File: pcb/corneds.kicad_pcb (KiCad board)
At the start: 2 copper layers, 320 x 105.6 mm, 124 parts, among them J3 AudioJack4, J4 AudioJack4, SW1 SW_Push, SW10 SW_Push, SW11 SW_Push, SW12 SW_Push, SW13 SW_Push, SW14 SW_Push, SW15 SW_Push, SW16 SW_Push, SW17 SW_Push, SW18 SW_Push, SW19 SW_Push, SW2 SW_Push, SW20 SW_Push, SW21 SW_Push, SW22 SW_Push, SW23 SW_Push, SW24 SW_Push, SW25 SW_Push, SW26 SW_Push, SW27 SW_Push, SW28 SW_Push, SW29 SW_Push, SW3 SW_Push, SW30 SW_Push, SW31 SW_Push, SW32 SW_Push, SW33 SW_Push, SW34 SW_Push, SW35 SW_Push, SW36 SW_Push, SW37 SW_Push, SW38 SW_Push, SW39 SW_Push, SW4 SW_Push, SW40 SW_Push, SW41 SW_Push, SW42 SW_Push, SW5 SW_Push, SW6 SW_Push, SW7 SW_Push, SW8 SW_Push, SW9 SW_Push, U1 Pico, U2 Pico, U3 SWD_Connector_3pin, U4 SWD_Connector_3pin, U5 Debug_UART_l, U6 Debug_UART_r

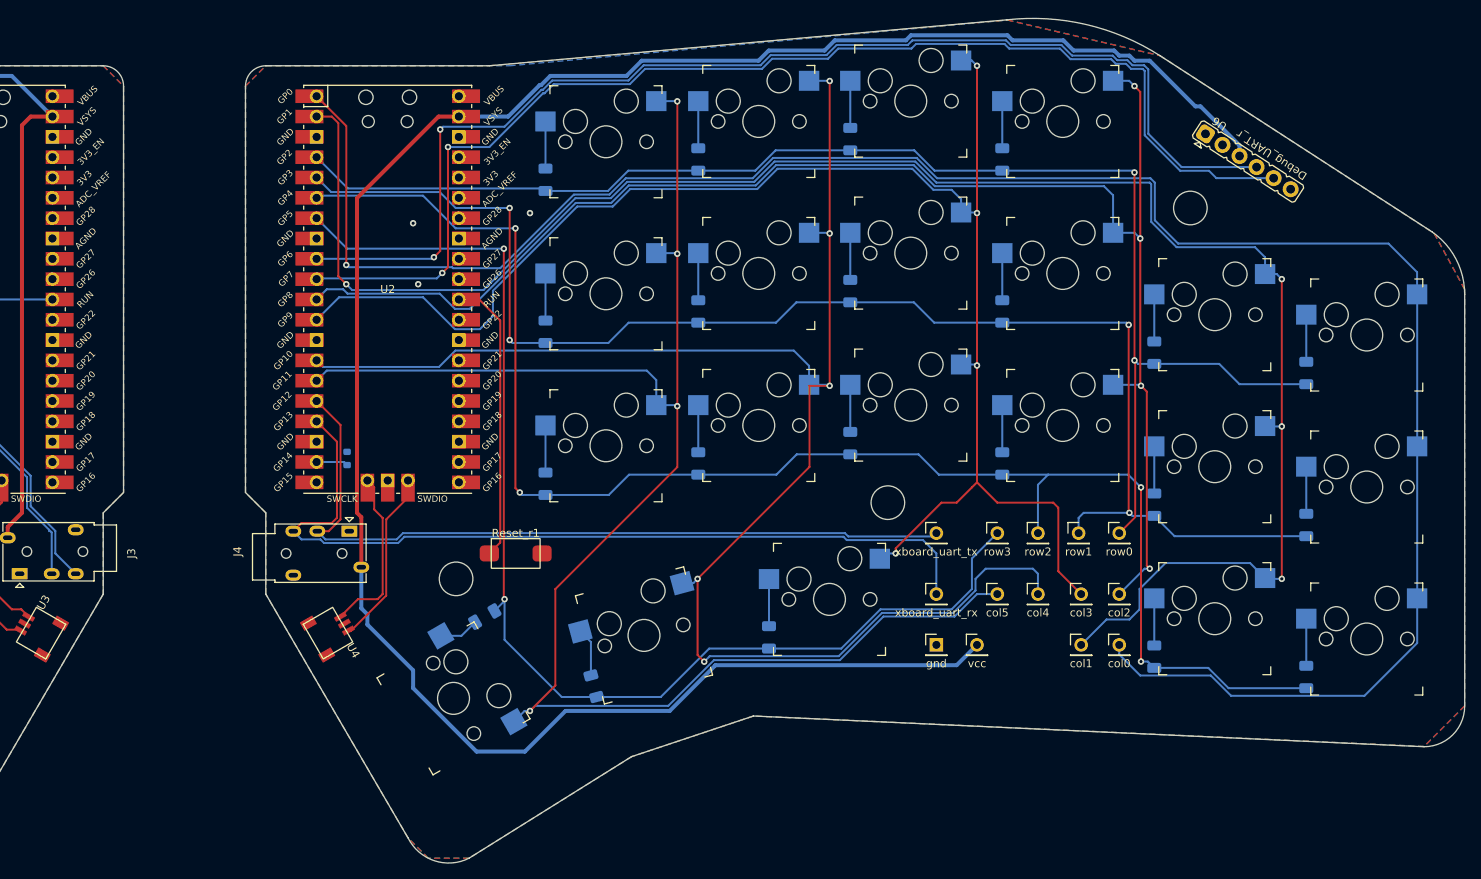
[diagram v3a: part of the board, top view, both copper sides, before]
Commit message: added tabs to rev3 and potentially fixed some pin swaps I missed. Also adding alt and gui to key mods
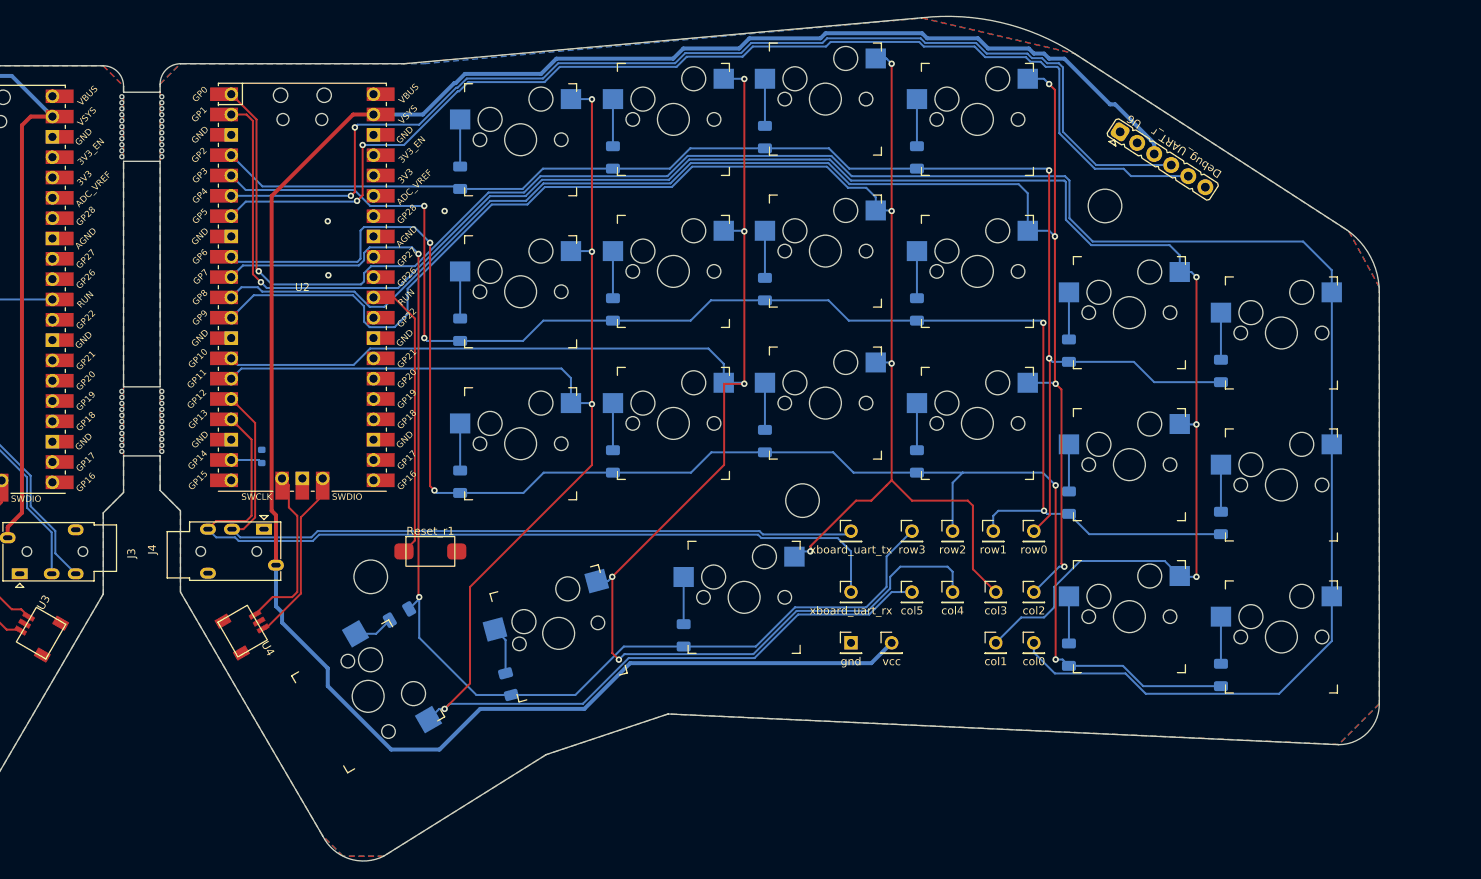
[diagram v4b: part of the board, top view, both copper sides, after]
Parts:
- added mouse-bite-5mm-slot: VAL**, Panelization:mouse-bite-5mm-slot, F.Cu at (139.4, 45.7)
- added mouse-bite-5mm-slot: VAL**, Panelization:mouse-bite-5mm-slot, F.Cu at (139.4, 82.5)
- moved D10 10.7 mm to (255.3, 73.7)
- moved D11 10.7 mm to (255.3, 92.7)
- moved D12 10.7 mm to (255.3, 111.7)
- moved D16 10.7 mm to (236.3, 49.6)
- moved D17 10.7 mm to (236.3, 68.6)
- moved D18 10.7 mm to (236.3, 87.6)
- moved D23 10.7 mm to (217.3, 47.0)
- moved D24 10.7 mm to (217.3, 66.0)
- moved D25 10.7 mm to (217.3, 85.0)
- moved D26 10.7 mm to (207.2, 109.3)
- moved D31 10.7 mm to (198.3, 49.6)
- moved D32 10.7 mm to (198.3, 68.6)
- moved D33 10.7 mm to (198.3, 87.6)
- moved D34 10.7 mm to (185.3, 115.4)
- moved D39 10.7 mm to (179.2, 52.1)
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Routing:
- net /dbg_uart_rx_r: track 152.3 -> 144.0 mm
- net /dbg_uart_tx_r: track 149.9 -> 141.6 mm
- net /col0_r: track 260.7 -> 264.0 mm
- net /col3_r: track 195.1 -> 196.2 mm
- net /row2_r: track 193.1 -> 194.2 mm
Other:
- board size 320 x 105.6 mm -> 309.4 x 105.8 mm
- board text added: "26 Nov 2023"
- board text removed: "21 Nov 2023"
